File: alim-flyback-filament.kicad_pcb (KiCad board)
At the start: 2 copper layers, 70 x 55 mm, 70 parts, among them Q1 IPD050N10N5, Q2 IPD050N10N5, T1 MSD1514-103ME, U1 UCC27517, U2 UCC27517, U3 ISO7710, U4 ISO7710, U5 DPC817, U7 AMC0311R, U8 AMC0311R, U9 AMC0302R

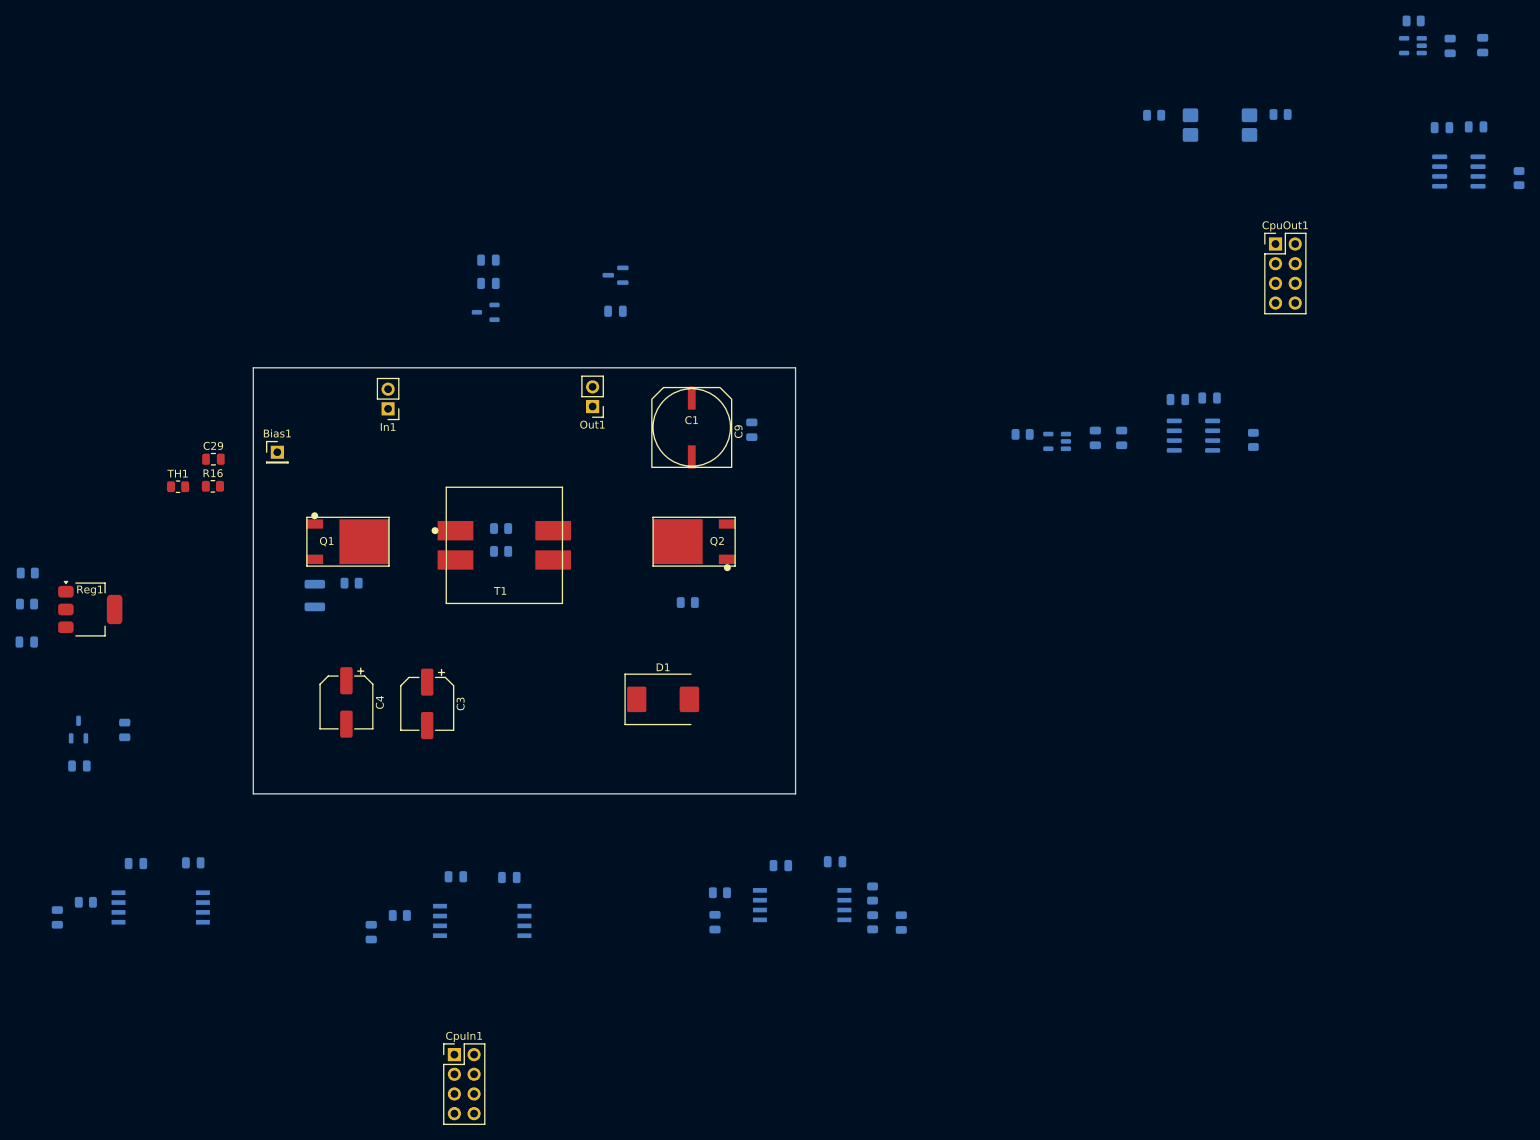
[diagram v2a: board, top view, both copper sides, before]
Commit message: Retours temperature/courant primaire isoles, isolation C2000 reelle, feuille Polarisation finalisee (80V, R26 corrige par simulation)
- U8 (AMC0311R) : retour temperature primaire (thermistance NTC) isole
- U9 (AMC0302R) : retour courant primaire (shunt R19) isole
- Migration GND_CTRL/3V3_CTRL : le C2000 externe recoit ses propres nets
  d'alimentation/masse isoles (U3/U4/U5/U7/U8/U9), connecteurs CpuOut/CpuIn
  agrandis a 16 broches
- Feuille polarisation.kicad_sch reprise en etiquettes globales uniquement
  (plus de fils explicites) et alignee sur la grille 1.27mm
- Source de courant Q3/Q4/R25/R26 simplifiee a un rail fixe 80V (HV80_IN,
  ex-400V) ; R26 corrige de 2M7 a 75k apres simulation SPICE (ngspice,
  modeles reels Diodes Inc.) qui a revele que le montage se comporte
  comme une resistance plutot qu'une source plate - voir 00-intention-
  conception.md §15bis
- Nouveau script bom_family_report.py (remplace BOMconverter.py) :
  nomenclature groupee par famille, sans dependance externe, lit soit le
  netlist XML legacy d'Eeschema soit un CSV kicad-cli
- README.md : image du schema integree
- Mise a jour 00-intention-conception.md (§13-15bis)

Co-Authored-By: Claude Sonnet 5 <noreply@anthropic.com>
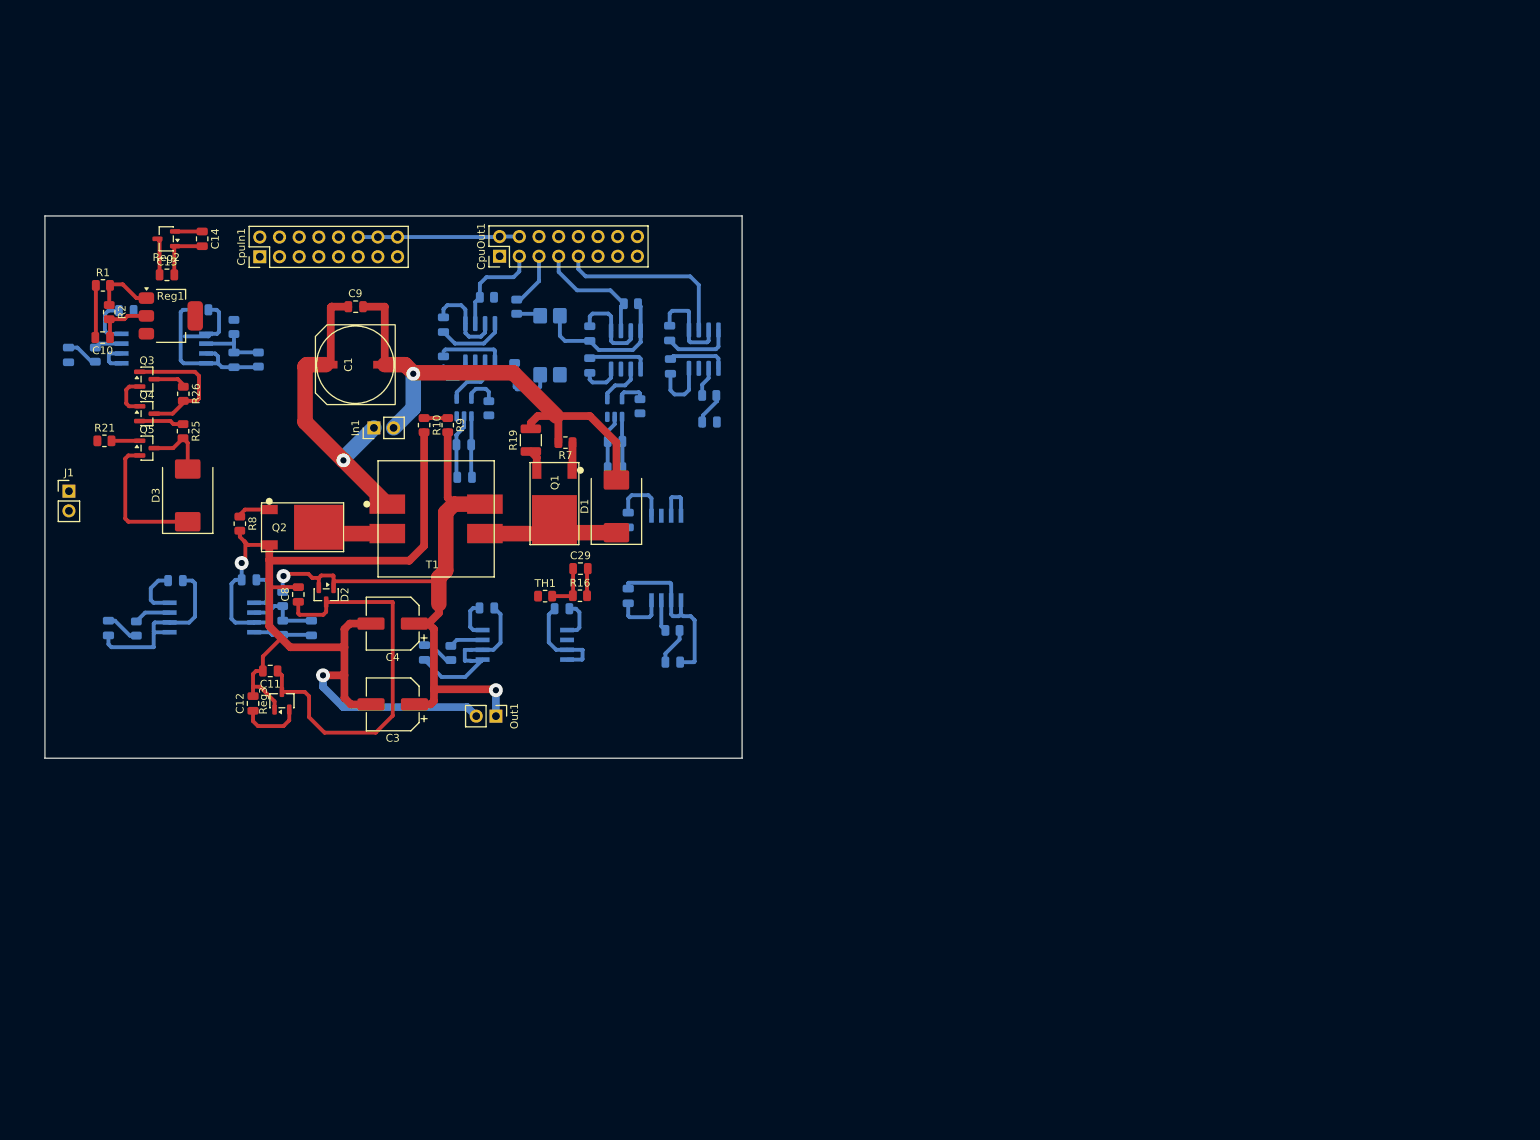
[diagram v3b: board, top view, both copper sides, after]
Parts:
- removed Bias1: HV_BIAS, Connector_PinHeader_2.54mm:PinHeader_1x01_P2.54mm_Vertical
- added C34: 100n, Capacitor_SMD:C_0805_2012Metric, B.Cu at (153.7, 75.5)
- added C35: 100n, Capacitor_SMD:C_0805_2012Metric, B.Cu at (153.8, 79.8)
- added C36: 100n, Capacitor_SMD:C_0805_2012Metric, B.Cu at (158.9, 87.0)
- added C38: 100n, Capacitor_SMD:C_0805_2012Metric, B.Cu at (93.3, 72.5)
- added C39: 100n, Capacitor_SMD:C_0805_2012Metric, B.Cu at (83.6, 72.6)
- added C40: 100p, Capacitor_SMD:C_0805_2012Metric, B.Cu at (97.5, 79.0)
- added C41: 1n, Capacitor_SMD:C_0805_2012Metric, B.Cu at (76.1, 78.3)
- added D3: SMCJ100A, Diode_SMD:D_SMC, F.Cu at (91.5, 96.5)
- added J1: HV80_IN, Connector_PinHeader_2.54mm:PinHeader_1x02_P2.54mm_Vertical, F.Cu at (76.2, 95.9)
- added Q3: BSS127I, Package_TO_SOT_SMD:SOT-23, F.Cu at (86.3, 81.5)
- added Q4: MMBT2222, Package_TO_SOT_SMD:SOT-23, F.Cu at (86.3, 85.9)
- added Q5: BSS127I, Package_TO_SOT_SMD:SOT-23, F.Cu at (86.3, 90.4)
- added R20: 10k, Resistor_SMD:R_0805_2012Metric, B.Cu at (158.9, 83.6)
- added R21: 1M, Resistor_SMD:R_0805_2012Metric, F.Cu at (80.8, 89.4)
- added R22: 470k, Resistor_SMD:R_0805_2012Metric, B.Cu at (97.5, 74.7)
- added R23: 10k, Resistor_SMD:R_0805_2012Metric, B.Cu at (100.7, 78.9)
- added R24: 100, Resistor_SMD:R_0805_2012Metric, B.Cu at (79.6, 78.3)
- added R25: 2k, Resistor_SMD:R_0805_2012Metric, F.Cu at (90.9, 88.2)
- added R26: 2M7, Resistor_SMD:R_0805_2012Metric, F.Cu at (91.0, 83.4)
- added U10: ISO7710, Package_SO:SOIC-8_3.9x4.9mm_P1.27mm, B.Cu at (158.1, 77.6)
- added U11: AMC0311R, SOIC_DWV:SOIC-8_DWV_5.85x11.5mm_P1.27mm, B.Cu at (88.5, 77.5)
- C10, C11, C12, C13, C14, C8, C9, D2, R1, R10, R19, R2, R7, R8, R9, Reg2, Reg3: moved to F.Cu
- CpuIn1, CpuOut1: footprint Connector_PinHeader_2.54mm:PinHeader_2x04_P2.54mm_Vertical -> Connector_PinHeader_2.54mm:PinHeader_2x08_P2.54mm_Vertical
- moved C21 142.8 mm to (127.3, 94.1), turned to 180 degrees
- moved C19 137.3 mm to (127.2, 89.9), turned to 180 degrees
- moved C16 136.8 mm to (124.5, 79.5), turned to 90 degrees
- moved R5 134.1 mm to (130.2, 70.9), turned to 0 degrees
- moved C15 131.4 mm to (124.5, 74.4), turned to -90 degrees
- moved U1 131.1 mm to (127.2, 85.1), turned to 90 degrees
- moved R11 129.4 mm to (130.4, 85.2), turned to -90 degrees
- moved U3 128.3 mm to (129.3, 76.8), turned to -90 degrees
- moved CpuIn1 106.0 mm to (100.8, 65.7), turned to 90 degrees
- moved R3 101.7 mm to (134.0, 72.1), turned to -90 degrees
- moved CpuOut1 100.2 mm to (131.8, 65.6), turned to 90 degrees
- moved U5 91.0 mm to (138.3, 77.1), turned to -90 degrees
- moved R4 88.9 mm to (133.7, 80.3), turned to -90 degrees
- moved C24 87.0 mm to (81.3, 113.6)
- moved C28 86.4 mm to (90.0, 107.5)
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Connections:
- U4 pad 3: RAIL_3V3_PRI -> 3V3_CTRL
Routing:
- net GND: track 0.00 -> 164.8 mm, vias 0 -> 1
- net VOUT_N: track 0.00 -> 162.7 mm, vias 0 -> 2
- net GND_CTRL: track 0.00 -> 132.3 mm
- net VOUT_P: track 0.00 -> 82.4 mm, vias 0 -> 2
- net 3V3_CTRL: track 0.00 -> 60.2 mm
- net VBOOT: track 0.00 -> 58.3 mm
- net VIN: track 0.00 -> 40.3 mm, vias 0 -> 1
- net RAIL_3V3_PRI: track 0.00 -> 38.7 mm
- net PWM_BIAS_IN: track 0.00 -> 23.9 mm
- net RAIL_8V25: track 0.00 -> 20.5 mm
- net RAIL_3V3_SEC: track 0.00 -> 18.8 mm
- net CS_GATE: track 0.00 -> 17.4 mm
- net SW_PRI: track 0.00 -> 17.0 mm
- net PWM_SEC_IN: track 0.00 -> 15.8 mm
- net PWM_PRI_IN: track 0.00 -> 13.1 mm
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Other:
- board size 70 x 55 mm -> 90 x 70 mm

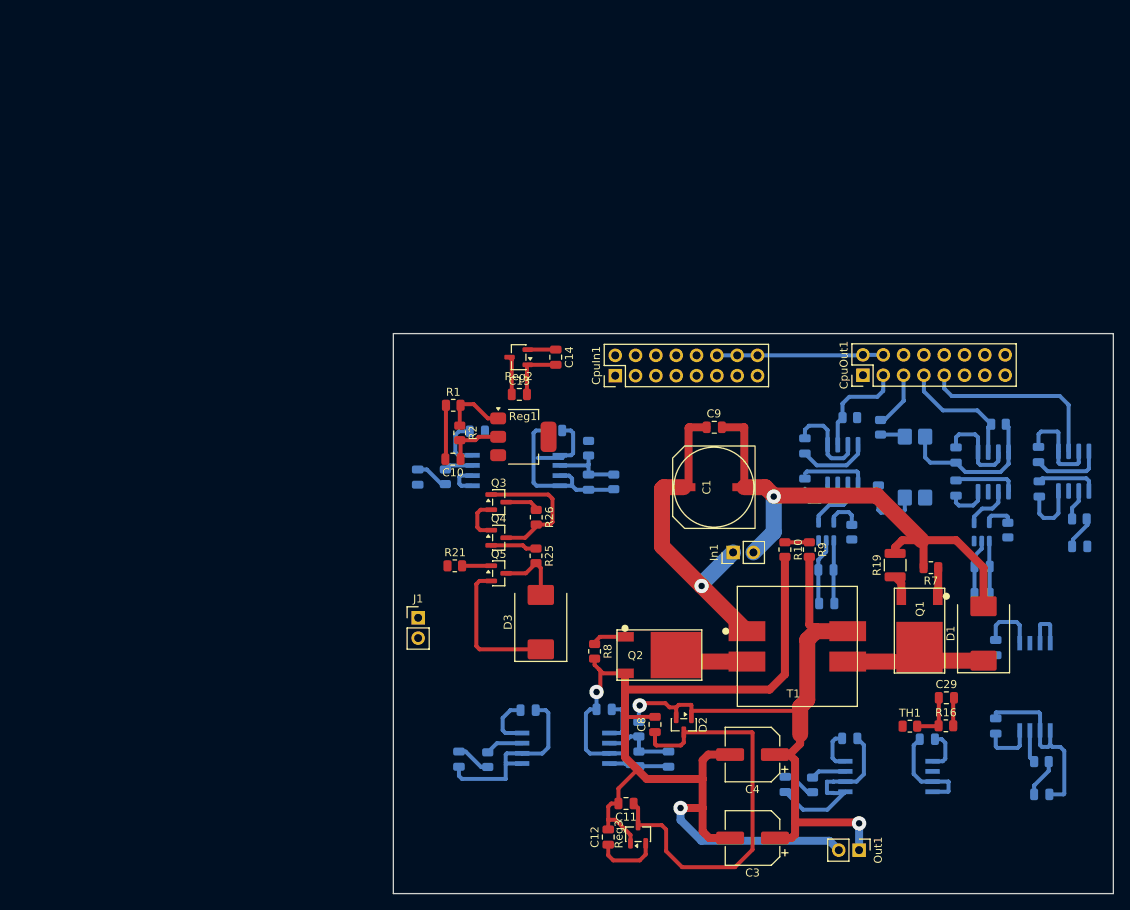
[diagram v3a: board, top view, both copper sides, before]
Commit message: Validation 18,9W + redressement synchrone : UCC24612 (U12) remplace U2/U4, clamp D4 ajouté
Simulation SPICE à la cible réelle (18,9W, pas les 10W de validation initiale) :
Vds_Q2 dépasse 100V dès Vin=20V sans clamp secondaire, indépendamment du
redresseur. UCC24612 amène +5pts de rendement mais ne corrige pas la
surtension -- D4 (SMCJ54A) ajouté pour ça. U2/U4 retirés (timing firmware
aveugle, remplacé par la détection Vds de l'UCC24612).

Co-Authored-By: Claude Sonnet 5 <noreply@anthropic.com>
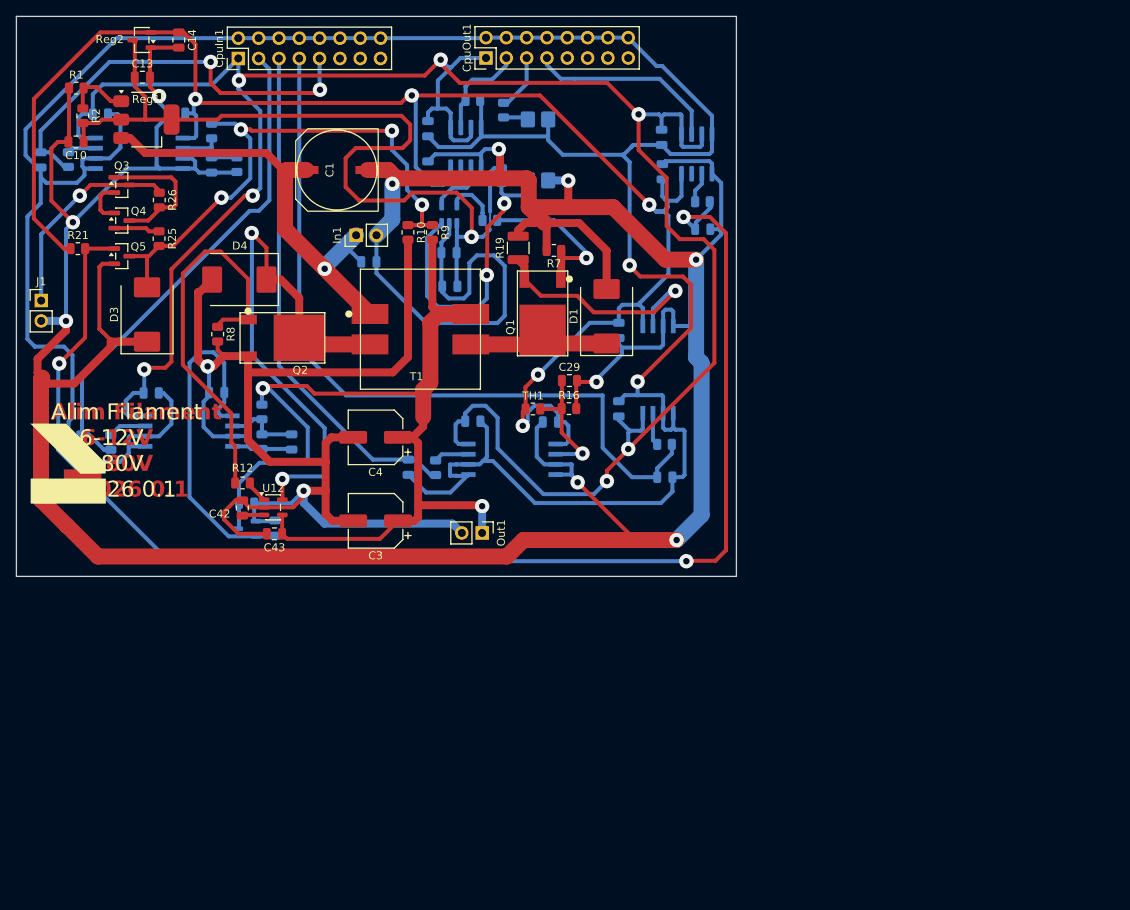
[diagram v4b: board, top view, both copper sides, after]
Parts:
- removed C11, C12: 1u, Capacitor_SMD:C_0805_2012Metric
- removed C17, C20, C27: 100n, Capacitor_SMD:C_0805_2012Metric
- removed C22: 10u, Capacitor_SMD:C_0805_2012Metric
- removed C8: 4u7, Capacitor_SMD:C_0805_2012Metric
- removed D2: BAT54C, Package_TO_SOT_SMD:SOT-23
- removed R6: 100k, Resistor_SMD:R_0805_2012Metric
- removed U2: UCC27517, Package_TO_SOT_SMD:SOT-23-5
- removed U4: ISO7710, Package_SO:SOIC-8_3.9x4.9mm_P1.27mm
- added ?: LOGO, lebel:lebel-logo, F.Cu at (32.8, 76.7)
- added ?: LOGO, lebel:lebel-logo_CU, F.Cu at (34.4, 76.4)
- added C42: 10u, Capacitor_SMD:C_0805_2012Metric, F.Cu at (54.2, 82.2)
- added C43: 100n, Capacitor_SMD:C_0805_2012Metric, F.Cu at (58.2, 85.4)
- added C44: 1u, Capacitor_SMD:C_0805_2012Metric, B.Cu at (54.8, 81.6)
- added C45: 1u, Capacitor_SMD:C_0805_2012Metric, B.Cu at (58.3, 84.7)
- added D4: SMCJ54A, Diode_SMD:D_SMC, F.Cu at (53.8, 53.6)
- added U12: UCC24612, Package_TO_SOT_SMD:SOT-23-5, F.Cu at (58.1, 82.1)
- C9, Reg3: moved to B.Cu
- R12: moved to F.Cu
- R26: value 2M7 -> 75k
- moved R12 95.8 mm to (54.3, 79.1), turned to 180 degrees
- moved C18 62.6 mm to (51.0, 67.8)
- moved D3 62.5 mm to (42.3, 58.0)
- moved Reg3 62.0 mm to (54.8, 84.8), turned to 180 degrees
- moved C36 61.6 mm to (111.8, 47.3)
- moved C39 61.6 mm to (36.5, 33.0)
- moved Out1 61.6 mm to (84.2, 85.3)
- moved R18 61.6 mm to (107.0, 74.3)
- moved U8 61.6 mm to (87.9, 76.1)
- moved C14 61.6 mm to (46.3, 23.7)
- moved C15 61.6 mm to (77.4, 34.8)
- moved C16 61.6 mm to (77.4, 39.8)
- moved C19 61.6 mm to (80.1, 50.3)
- moved C23 61.6 mm to (60.4, 73.9)
- moved C26 61.6 mm to (83.0, 71.4)
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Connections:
- CpuOut1 pad 7: PWM_SEC_IN -> PWM_BIAS_IN
- CpuOut1 pad 9: PWM_BIAS_IN -> unconnected-(CpuOut1-Pin_9-Pad9)
- Reg3 pad 3: VBOOT -> VOUT_P
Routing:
- net GND: track 164.8 -> 482.0 mm, vias 1 -> 10
- net 3V3_CTRL: track 60.2 -> 277.4 mm, vias 0 -> 7
- net GND_CTRL: track 132.3 -> 348.1 mm, vias 0 -> 2
- net RAIL_3V3_PRI: track 38.7 -> 205.1 mm, vias 0 -> 5
- net VAR_GATE: track 8.30 -> 173.0 mm, vias 0 -> 3
- net RAIL_8V25: track 20.5 -> 112.4 mm, vias 0 -> 1
- net ISENSE_PRI_FBACK: track 4.86 -> 96.4 mm
- net TEMP_PRI_FBACK: track 4.20 -> 63.6 mm
- net SW_SEC: track 9.18 -> 68.1 mm, vias 0 -> 2
- net HV_BIAS: track 11.2 -> 69.8 mm, vias 0 -> 4
- net VBOOT: track 58.3 -> 0.00 mm
- net VOUT_FBACK: track 4.40 -> 62.3 mm
- net BIAS_FBACK: track 4.21 -> 53.1 mm, vias 0 -> 2
- net GATE_Q2: track 4.31 -> 49.0 mm
- net VOUT_P: track 82.4 -> 125.3 mm
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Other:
- board text added: "Alim Filament 6-12V 0-80V 2026 0.1"
